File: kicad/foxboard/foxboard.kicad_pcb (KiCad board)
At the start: 2 copper layers, 40.2 x 15 mm, 184 parts, among them J2 USB_C_Receptacle_USB2.0, K1 KEYSW, K10 KEYSW, K11 KEYSW, K12 KEYSW, K13 KEYSW, K14 KEYSW, K15 KEYSW, K16 KEYSW, K17 KEYSW, K18 KEYSW, K19 KEYSW, K2 KEYSW, K20 KEYSW, K21 KEYSW, K22 KEYSW, K23 KEYSW, K24 KEYSW, K25 KEYSW, K26 KEYSW, K27 KEYSW, K28 KEYSW, K29 KEYSW, K3 KEYSW, K30 KEYSW, K31 KEYSW, K32 KEYSW, K33 KEYSW, K34 KEYSW, K35 KEYSW, K36 KEYSW, K38 KEYSW, K39 KEYSW, K4 KEYSW, K40 KEYSW, K41 KEYSW, K42 KEYSW, K43 KEYSW, K44 KEYSW, K45 KEYSW, K46 KEYSW, K47 KEYSW, K48 KEYSW, K49 KEYSW, K5 KEYSW, K50 KEYSW, K51 KEYSW, K52 KEYSW, K53 KEYSW, K54 KEYSW, K55 KEYSW, K56 KEYSW, K57 KEYSW, K58 KEYSW, K59 KEYSW, K6 KEYSW, K60 KEYSW, K61 KEYSW, K62 KEYSW, K63 KEYSW, K64 KEYSW, K65 KEYSW, K66 KEYSW, K67 KEYSW, K68 KEYSW, K69 KEYSW, K7 KEYSW, K70 KEYSW, K71 KEYSW, K72 KEYSW, K73 KEYSW, K74 KEYSW, K75 KEYSW, K76 KEYSW, K77 KEYSW, K78 KEYSW, K79 KEYSW, K8 KEYSW, K80 KEYSW, K81 KEYSW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

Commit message: add few cols & update eeschema
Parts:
- removed the D37 at (257.0, 297.2)
- added K37: KEYSW, PCM_marbastlib-mx:SW_MX_1u, F.Cu at (241.3, 307.3)
- added REF**: STAB_MX_2u, PCM_marbastlib-mx:STAB_MX_2u, F.Cu at (243.8, 266.7)
- added REF**: STAB_MX_2.25u, PCM_marbastlib-mx:STAB_MX_2.25u, F.Cu at (241.3, 304.8)
- added REF**: STAB_MX_2.25u, PCM_marbastlib-mx:STAB_MX_2.25u, F.Cu at (-2.54, 325.1)
- added REF**: STAB_MX_2.75u, PCM_marbastlib-mx:STAB_MX_2.75u, F.Cu at (236.2, 325.1)
- D37: moved to B.Cu
- K12, K23: footprint PCM_marbastlib-xp-plate-mx:Plate_MX_SPLIT-RSHIFT -> PCM_marbastlib-mx:SW_MX_1u
- K25: footprint PCM_marbastlib-mx:STAB_MX_2.25u -> PCM_marbastlib-mx:SW_MX_1u
- K69: footprint PCM_marbastlib-mx:STAB_MX_2.75u -> PCM_marbastlib-mx:SW_MX_1u
- moved D37 393.8 mm to (257.0, 299.7), turned to 180 degrees
- moved K12 2.54 mm to (-2.54, 325.1)
- moved K38 1.07 mm to (-10.2, 287.1)
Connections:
- K10 pad 1: Net-(K10-Pad1) -> Net-(U2-36_CS)
- K24 pad 1: Net-(K10-Pad1) -> Net-(U2-36_CS)
- K36 pad 1: Net-(K23-Pad1) -> Net-(U2-39_MISO1_OUT1A)
- K38 pad 1: Net-(K13-Pad1) -> Net-(K1-Pad1)
- K39 pad 1: Net-(K14-Pad1) -> Net-(K13-Pad1)
- K49 pad 1: Net-(K23-Pad1) -> Net-(U2-39_MISO1_OUT1A)
- K50 pad 1: Net-(K37-Pad1) -> Net-(U2-29_TX7)
- K51 pad 1: Net-(K51-Pad1) -> Net-(U2-38_CS1_IN1)
- K52 pad 1: Net-(K52-Pad1) -> Net-(U2-37_CS)
- K53 pad 1: Net-(K10-Pad1) -> Net-(U2-36_CS)
- K54 pad 1: Net-(K1-Pad1) -> Net-(U2-35_TX8)
- K55 pad 1: Net-(K13-Pad1) -> Net-(K1-Pad1)
- K56 pad 1: Net-(K14-Pad1) -> Net-(K13-Pad1)
- K66 pad 1: Net-(K23-Pad1) -> Net-(U2-39_MISO1_OUT1A)
- K67 pad 1: Net-(K37-Pad1) -> Net-(U2-29_TX7)
- K68 pad 1: Net-(K51-Pad1) -> Net-(U2-36_CS)
- K8 pad 1: Net-(K23-Pad1) -> Net-(U2-39_MISO1_OUT1A)
- K81 pad 1: unconnected-(K81-Pad1) -> Net-(U2-39_MISO1_OUT1A)
- K82 pad 1: unconnected-(K82-Pad1) -> Net-(U2-29_TX7)
- K83 pad 1: Net-(K51-Pad1) -> Net-(U2-38_CS1_IN1)
- K84 pad 1: Net-(K52-Pad1) -> Net-(U2-37_CS)
- K85 pad 1: Net-(K10-Pad1) -> Net-(U2-36_CS)
- K87 pad 1: Net-(K52-Pad1) -> Net-(U2-37_CS)
- K9 pad 1: Net-(K52-Pad1) -> Net-(U2-37_CS)
- U2 pad 21: unconnected-(U2-29_TX7-Pad21) -> Net-(U2-29_TX7)
- U2 pad 28: unconnected-(U2-36_CS-Pad28) -> Net-(U2-36_CS)
- U2 pad 29: unconnected-(U2-37_CS-Pad29) -> Net-(U2-37_CS)
- U2 pad 30: unconnected-(U2-38_CS1_IN1-Pad30) -> Net-(U2-38_CS1_IN1)
- U2 pad 31: unconnected-(U2-39_MISO1_OUT1A-Pad31) -> Net-(U2-39_MISO1_OUT1A)
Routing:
- net Net-(U2-39_MISO1_OUT1A): track 0.00 -> 304.2 mm
- net Net-(U2-29_TX7): track 0.00 -> 177.7 mm
- net Net-(U2-37_CS): track 0.00 -> 174.4 mm
- net Net-(U2-38_CS1_IN1): track 0.00 -> 156.2 mm
- net Net-(U2-36_CS): track 0.00 -> 153.0 mm
- net Net-(K13-Pad1): track 0.00 -> 131.7 mm
- net Net-(K14-Pad1): track 0.00 -> 127.9 mm
- net Net-(K1-Pad1): track 0.00 -> 114.4 mm
- net Net-(U2-35_TX8): track 28.7 -> 116.7 mm
- net Net-(K15-Pad1): track 0.00 -> 67.1 mm
- net Net-(D23-A): track 0.00 -> 22.8 mm
- net Net-(D38-K): track 368.0 -> 366.4 mm
- net Net-(D71-K): track 450.5 -> 451.4 mm
- net Net-(D25-K): track 311.4 -> 310.9 mm
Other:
- board outline removed

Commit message: add finish cols and usbc & update eeschema
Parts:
- removed C3, C4, C5, C6: 0.1u, Capacitor_SMD:C_0201_0603Metric_Pad0.64x0.40mm_HandSolder
- removed C7: 4.7u, Capacitor_SMD:C_0201_0603Metric_Pad0.64x0.40mm_HandSolder
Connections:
- K1 pad 1: Net-(K1-Pad1) -> Net-(U2-12_MISO_MQSL)
- K12 pad 1: Net-(K1-Pad1) -> Net-(U2-12_MISO_MQSL)
- K13 pad 1: Net-(K13-Pad1) -> Net-(U2-14_A0_TX3_SPDIF_OUT)
- K14 pad 1: Net-(K14-Pad1) -> Net-(U2-13_SCK_LED)
- K17 pad 1: Net-(K17-Pad1) -> Net-(U2-41_A17)
- K18 pad 1: Net-(K18-Pad1) -> Net-(U2-24_A10_TX6_SCL2)
- K19 pad 1: Net-(K19-Pad1) -> Net-(U2-40_A16)
- K2 pad 1: Net-(K13-Pad1) -> Net-(U2-14_A0_TX3_SPDIF_OUT)
- K20 pad 1: Net-(K20-Pad1) -> Net-(U2-39_MISO1_OUT1A)
- K21 pad 1: Net-(K21-Pad1) -> Net-(U2-26_A12_MOSI1)
- K22 pad 1: Net-(K22-Pad1) -> Net-(U2-27_A13_SCK1)
- K23 pad 1: Net-(U2-39_MISO1_OUT1A) -> Net-(U2-28_RX7)
- K25 pad 1: Net-(K1-Pad1) -> Net-(U2-12_MISO_MQSL)
- K26 pad 1: Net-(K13-Pad1) -> Net-(U2-14_A0_TX3_SPDIF_OUT)
- K27 pad 1: Net-(K14-Pad1) -> Net-(U2-13_SCK_LED)
- K3 pad 1: Net-(K14-Pad1) -> Net-(U2-13_SCK_LED)
- K30 pad 1: Net-(K17-Pad1) -> Net-(U2-41_A17)
- K31 pad 1: Net-(K18-Pad1) -> Net-(U2-24_A10_TX6_SCL2)
- K32 pad 1: Net-(K19-Pad1) -> Net-(U2-40_A16)
- K33 pad 1: Net-(K20-Pad1) -> Net-(U2-39_MISO1_OUT1A)
- K34 pad 1: Net-(K21-Pad1) -> Net-(U2-26_A12_MOSI1)
- K35 pad 1: Net-(K22-Pad1) -> Net-(U2-27_A13_SCK1)
- K36 pad 1: Net-(U2-39_MISO1_OUT1A) -> Net-(U2-28_RX7)
- K38 pad 1: Net-(K1-Pad1) -> Net-(U2-12_MISO_MQSL)
- K39 pad 1: Net-(K13-Pad1) -> Net-(U2-14_A0_TX3_SPDIF_OUT)
- K4 pad 1: Net-(K17-Pad1) -> Net-(U2-41_A17)
- K40 pad 1: Net-(K14-Pad1) -> Net-(U2-13_SCK_LED)
- K43 pad 1: Net-(K17-Pad1) -> Net-(U2-41_A17)
- K44 pad 1: Net-(K18-Pad1) -> Net-(U2-24_A10_TX6_SCL2)
- K45 pad 1: Net-(K19-Pad1) -> Net-(U2-40_A16)
- K46 pad 1: Net-(K20-Pad1) -> Net-(U2-39_MISO1_OUT1A)
- K47 pad 1: Net-(K21-Pad1) -> Net-(U2-26_A12_MOSI1)
- K48 pad 1: Net-(K22-Pad1) -> Net-(U2-27_A13_SCK1)
- K49 pad 1: Net-(U2-39_MISO1_OUT1A) -> Net-(U2-28_RX7)
- K5 pad 1: Net-(K20-Pad1) -> Net-(U2-39_MISO1_OUT1A)
- K55 pad 1: Net-(K1-Pad1) -> Net-(U2-12_MISO_MQSL)
- K56 pad 1: Net-(K13-Pad1) -> Net-(U2-14_A0_TX3_SPDIF_OUT)
- K57 pad 1: Net-(K14-Pad1) -> Net-(U2-13_SCK_LED)
- K6 pad 1: Net-(K21-Pad1) -> Net-(U2-26_A12_MOSI1)
- K60 pad 1: Net-(K17-Pad1) -> Net-(U2-41_A17)
- K61 pad 1: Net-(K18-Pad1) -> Net-(U2-24_A10_TX6_SCL2)
- K62 pad 1: Net-(K19-Pad1) -> Net-(U2-40_A16)
- K63 pad 1: Net-(K20-Pad1) -> Net-(U2-39_MISO1_OUT1A)
- K64 pad 1: Net-(K21-Pad1) -> Net-(U2-26_A12_MOSI1)
- K65 pad 1: Net-(K22-Pad1) -> Net-(U2-27_A13_SCK1)
- K66 pad 1: Net-(U2-39_MISO1_OUT1A) -> Net-(U2-28_RX7)
- K7 pad 1: Net-(K22-Pad1) -> Net-(U2-27_A13_SCK1)
- K71 pad 1: Net-(K1-Pad1) -> Net-(U2-12_MISO_MQSL)
- K72 pad 1: Net-(K13-Pad1) -> Net-(U2-14_A0_TX3_SPDIF_OUT)
- K73 pad 1: Net-(K14-Pad1) -> Net-(U2-13_SCK_LED)
- K75 pad 1: Net-(K17-Pad1) -> Net-(U2-41_A17)
- K76 pad 1: Net-(K18-Pad1) -> Net-(U2-24_A10_TX6_SCL2)
- K77 pad 1: Net-(K19-Pad1) -> Net-(U2-40_A16)
- K78 pad 1: Net-(K20-Pad1) -> Net-(U2-39_MISO1_OUT1A)
- K79 pad 1: Net-(K21-Pad1) -> Net-(U2-26_A12_MOSI1)
- K8 pad 1: Net-(U2-39_MISO1_OUT1A) -> Net-(U2-28_RX7)
- K80 pad 1: Net-(K22-Pad1) -> Net-(U2-27_A13_SCK1)
- K81 pad 1: Net-(U2-39_MISO1_OUT1A) -> Net-(U2-28_RX7)
- U2 pad 14: unconnected-(U2-12_MISO_MQSL-Pad14) -> Net-(U2-12_MISO_MQSL)
- U2 pad 15: unconnected-(U2-3V3-Pad15) -> Net-(K15-Pad1)
- U2 pad 16: unconnected-(U2-24_A10_TX6_SCL2-Pad16) -> Net-(U2-24_A10_TX6_SCL2)
- U2 pad 18: unconnected-(U2-26_A12_MOSI1-Pad18) -> Net-(U2-26_A12_MOSI1)
- U2 pad 19: unconnected-(U2-27_A13_SCK1-Pad19) -> Net-(U2-27_A13_SCK1)
- U2 pad 20: unconnected-(U2-28_RX7-Pad20) -> Net-(U2-28_RX7)
- U2 pad 32: unconnected-(U2-40_A16-Pad32) -> Net-(U2-40_A16)
- U2 pad 33: unconnected-(U2-41_A17-Pad33) -> Net-(U2-41_A17)
- U2 pad 34: unconnected-(U2-GND-Pad34) -> Net-(K16-Pad1)
- U2 pad 35: unconnected-(U2-13_SCK_LED-Pad35) -> Net-(U2-13_SCK_LED)
- U2 pad 36: unconnected-(U2-14_A0_TX3_SPDIF_OUT-Pad36) -> Net-(U2-14_A0_TX3_SPDIF_OUT)
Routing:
- net Net-(J2-D+-PadA6): track 0.00 -> 914.7 mm, vias 0 -> 5
- net Net-(J2-D--PadA7): track 0.00 -> 485.6 mm, vias 0 -> 3
- net Net-(U2-14_A0_TX3_SPDIF_OUT): track 0.00 -> 478.1 mm, vias 0 -> 2
- net Net-(U2-13_SCK_LED): track 0.00 -> 467.3 mm, vias 0 -> 1
- net Net-(U2-12_MISO_MQSL): track 0.00 -> 452.4 mm, vias 0 -> 4
- net Net-(U2-41_A17): track 0.00 -> 429.7 mm, vias 0 -> 3
- net Net-(U2-40_A16): track 0.00 -> 401.7 mm, vias 0 -> 1
- net Net-(J2-SHIELD): track 0.00 -> 367.8 mm, vias 0 -> 4
- net Net-(U2-VIN): track 0.00 -> 361.1 mm, vias 0 -> 7
- net Net-(U2-24_A10_TX6_SCL2): track 0.00 -> 294.8 mm, vias 0 -> 1
- net Net-(U2-26_A12_MOSI1): track 0.00 -> 254.0 mm, vias 0 -> 2
- net Net-(K16-Pad1): track 95.7 -> 342.0 mm, vias 0 -> 2
- net Net-(K15-Pad1): track 67.1 -> 313.0 mm, vias 0 -> 2
- net Net-(U2-27_A13_SCK1): track 0.00 -> 238.6 mm, vias 0 -> 2
- net Net-(U2-28_RX7): track 0.00 -> 228.8 mm, vias 0 -> 2
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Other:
- board outline added: 365.8 x 142.2 mm
- board text removed: "FoxBoard by Lunarequest"

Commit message: move teensy a little back
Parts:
- moved U2 2.86 mm to (295.6, 306.1)
- moved REF** 0.63 mm to (236.2, 324.5)
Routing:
- net Net-(U2-37_CS): track 174.4 -> 483.7 mm
- net Net-(D37-A): track 0.00 -> 13.8 mm
- net Net-(D25-K): track 310.9 -> 320.9 mm
- net Net-(U2-35_TX8): track 116.7 -> 123.5 mm
- net Net-(D36-A): track 0.00 -> 6.77 mm
- net Net-(D1-K): track 356.0 -> 362.6 mm
- net Net-(D66-A): track 0.00 -> 5.72 mm
- net Net-(U2-28_RX7): track 228.8 -> 223.8 mm
- net Net-(J2-D--PadA7): track 485.6 -> 481.1 mm
- net Net-(D38-K): track 367.8 -> 372.3 mm, vias 0 -> 2
- net Net-(U2-29_TX7): track 177.7 -> 181.8 mm
- net Net-(D12-K): track 314.5 -> 318.5 mm
- net Net-(D69-A): track 0.00 -> 3.60 mm
- net Net-(D55-K): track 383.4 -> 386.9 mm
- net Net-(U2-12_MISO_MQSL): track 452.4 -> 455.4 mm
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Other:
- outline, holes or cut-outs redrawn

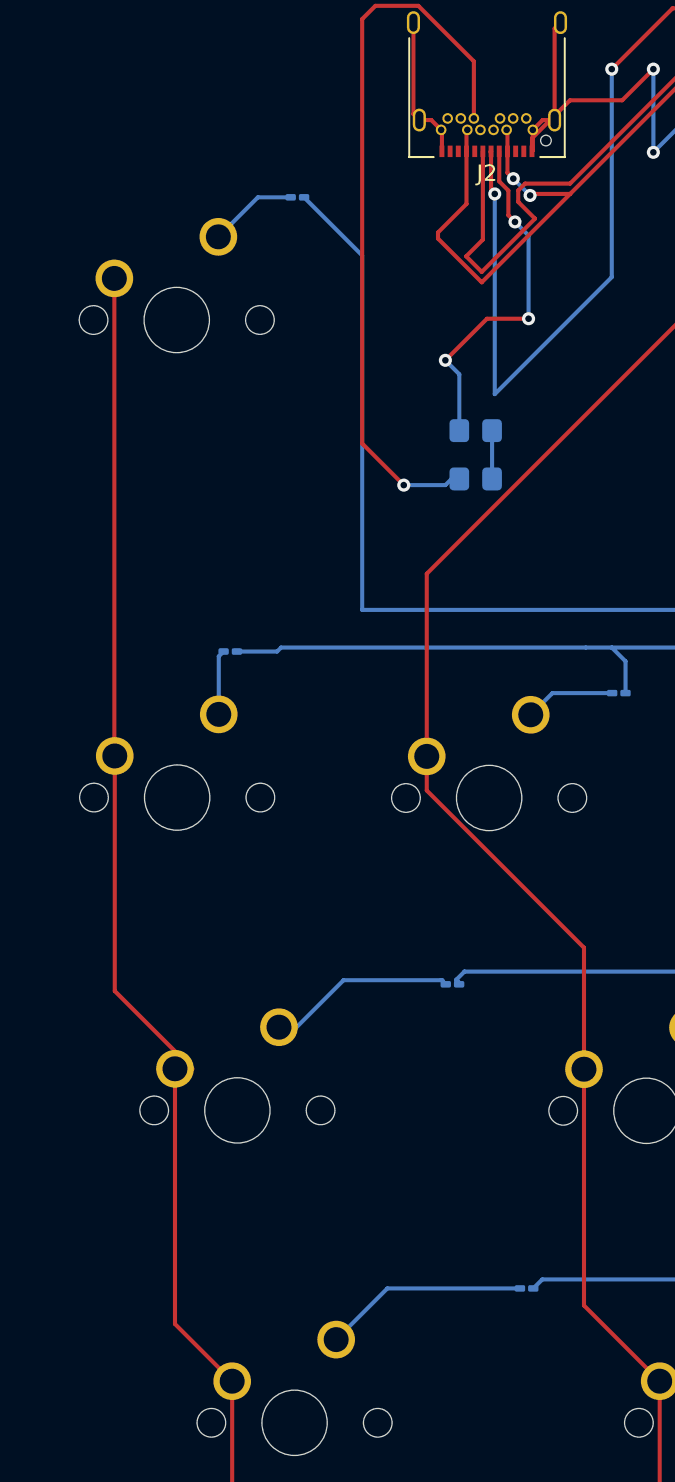
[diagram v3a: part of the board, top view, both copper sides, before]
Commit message: hook up resistor to ground
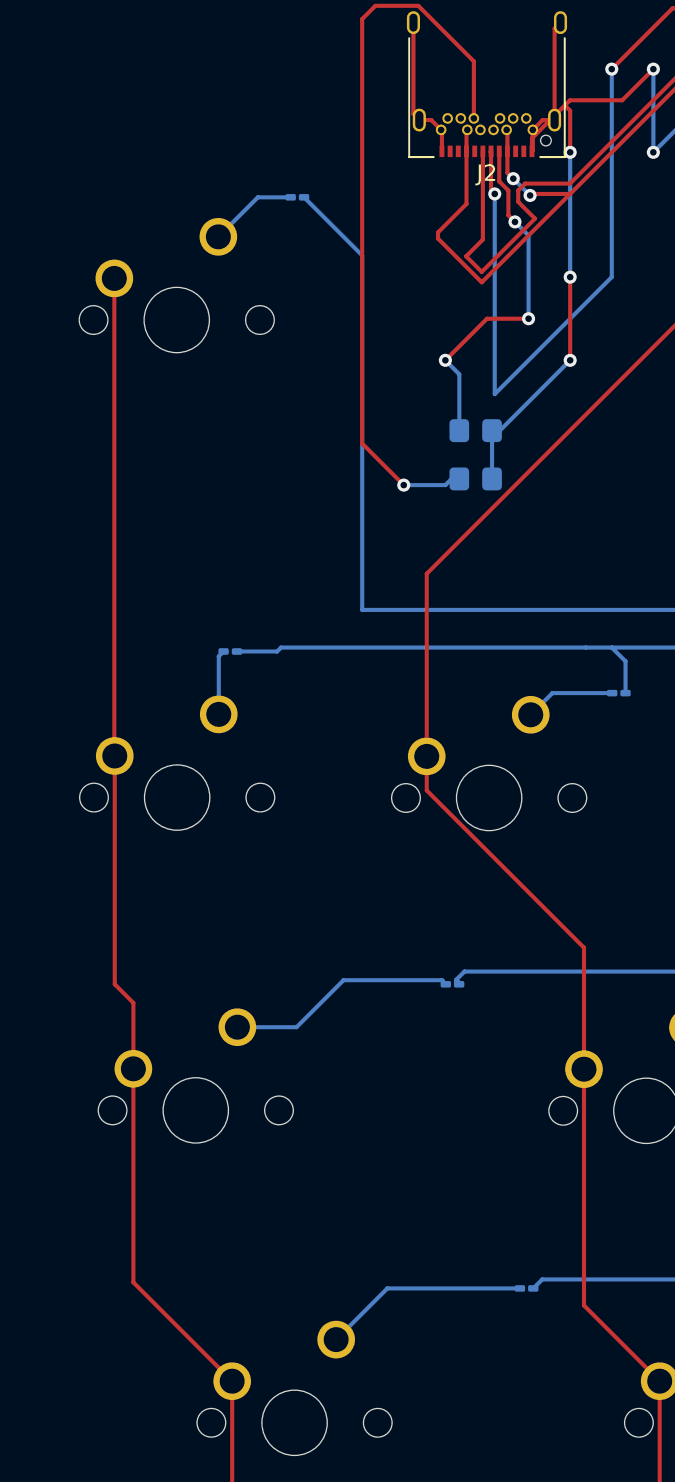
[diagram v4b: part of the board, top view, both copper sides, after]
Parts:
- moved K38 2.54 mm to (-12.7, 287.1)
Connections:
- net Net-(U2-VIN) renamed VBUS
- J2 pad A1: Net-(J2-SHIELD) -> GND
- J2 pad A12: Net-(J2-SHIELD) -> GND
- J2 pad B1: Net-(J2-SHIELD) -> GND
- J2 pad B12: Net-(J2-SHIELD) -> GND
- J2 pad S1: Net-(J2-SHIELD) -> GND
- K52 pad 1: Net-(U2-37_CS) -> Net-(D9-A)
- K84 pad 1: Net-(U2-37_CS) -> Net-(D9-A)
- K87 pad 1: Net-(U2-37_CS) -> Net-(D9-A)
- K9 pad 1: Net-(U2-37_CS) -> Net-(D9-A)
- R5 pad 1: +5V -> GND
- R5 pad 2: Net-(J2-CC1) -> Net-(J2-CC2)
- R6 pad 1: +5V -> GND
- R6 pad 2: Net-(J2-CC2) -> Net-(J2-CC1)
- U2 pad 29: Net-(U2-37_CS) -> Net-(D9-A)
- U2 pad 47: Net-(J2-SHIELD) -> GND
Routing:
- net Net-(U2-37_CS): track 483.7 -> 0.00 mm
- net Net-(D9-A): track 5.52 -> 489.2 mm
- net GND: track 0.00 -> 394.0 mm, vias 0 -> 7
- net Net-(J2-SHIELD): track 368.6 -> 0.00 mm, vias 4 -> 0
- net Net-(D38-A): track 10.5 -> 14.1 mm
- net +5V: track 3.14 -> 0.00 mm

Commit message: switch to better layout
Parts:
- removed REF**: STAB_MX_6.25u, PCM_marbastlib-mx:STAB_MX_6.25u
- removed REF**: STAB_MX_2u, PCM_marbastlib-mx:STAB_MX_2u
- removed REF** (x2): STAB_MX_2.25u, PCM_marbastlib-mx:STAB_MX_2.25u
- removed REF**: STAB_MX_2.75u, PCM_marbastlib-mx:STAB_MX_2.75u
- added S30: BACKSPACE, PCM_marbastlib-mx:STAB_MX_2u, F.Cu at (283.8, 275.0)
- added S63: ANSI_ENTER, PCM_marbastlib-mx:STAB_MX_2.25u, F.Cu at (281.5, 313.1)
- added S64: LShift, PCM_marbastlib-mx:STAB_MX_2.25u, F.Cu at (38.6, 332.1)
- added S75: RSHIFT, PCM_marbastlib-mx:STAB_MX_P_2.75u, F.Cu at (276.7, 332.1)
- added S80: 7u_SPACE, PCM_marbastlib-mx:STAB_MX_P_6.25u, F.Cu at (148.1, 351.2)
- K1, K2, K3, K5, K6, K7, K8: footprint PCM_marbastlib-mx:SW_MX_1.25u -> PCM_marbastlib-mx:SW_MX_1u
- K15, K77, K78, K79, K81, K82, K83, K9: footprint PCM_marbastlib-mx:SW_MX_1u -> PCM_marbastlib-mx:SW_MX_1.25u
- K34, K47: footprint PCM_marbastlib-mx:SW_MX_1u -> PCM_marbastlib-mx:SW_MX_1.5u
- K38: footprint PCM_marbastlib-mx:SW_MX_1.75u -> PCM_marbastlib-mx:SW_MX_1u
- K4: footprint rhais_cherry:MX_KEY_4.45 -> PCM_marbastlib-mx:SW_MX_1u
- U2: moved to B.Cu
- moved K12 287.8 mm to (274.3, 246.4)
- moved K16 280.4 mm to (355.3, 246.4)
- moved K15 280.3 mm to (336.2, 246.4)
- moved K14 280.2 mm to (317.2, 246.4)
- moved D16 279.5 mm to (361.9, 238.7)
- moved D14 279.4 mm to (323.8, 238.7)
- moved D15 279.3 mm to (342.9, 238.7)
- moved D12 276.7 mm to (281.0, 238.7)
- moved K13 275.7 mm to (293.4, 246.4)
- moved D13 275.5 mm to (300.0, 238.7)
- moved K76 244.5 mm to (336.2, 332.1)
- moved D76 243.4 mm to (342.9, 324.4)
- moved D51 219.8 mm to (40.5, 305.4)
- moved K71 218.6 mm to (183.8, 332.1)
- moved K53 218.2 mm to (79.1, 313.1)
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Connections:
- D1 pad 1: Net-(D1-K) -> row 1
- D10 pad 1: Net-(D1-K) -> row 1
- D11 pad 1: Net-(D1-K) -> row 1
- D12 pad 1: Net-(D12-K) -> row 1
- D13 pad 1: Net-(D12-K) -> row 1
- D14 pad 1: Net-(D12-K) -> row 1
- D15 pad 1: Net-(D12-K) -> row 1
- D16 pad 1: Net-(D12-K) -> row 1
- D17 pad 1: Net-(D12-K) -> row 2
- D18 pad 1: Net-(D12-K) -> row 2
- D19 pad 1: Net-(D12-K) -> row 2
- D2 pad 1: Net-(D1-K) -> row 1
- D20 pad 1: Net-(D12-K) -> row 2
- D21 pad 1: Net-(D12-K) -> row 2
- D22 pad 1: Net-(D12-K) -> row 2
- D23 pad 1: Net-(D12-K) -> row 2
- D24 pad 1: Net-(D12-K) -> row 2
- D25 pad 1: Net-(D25-K) -> row 2
- D26 pad 1: Net-(D25-K) -> row 2
- D27 pad 1: Net-(D25-K) -> row 2
- D28 pad 1: Net-(D25-K) -> row 2
- D29 pad 1: Net-(D25-K) -> row 2
- D3 pad 1: Net-(D1-K) -> row 1
- D30 pad 1: Net-(D25-K) -> row 2
- D31 pad 1: Net-(D25-K) -> row 2
- D32 pad 1: Net-(D25-K) -> row 2
- D33 pad 1: Net-(D25-K) -> row 2
- D34 pad 1: Net-(D25-K) -> row 3
- D35 pad 1: Net-(D25-K) -> row 3
- D36 pad 1: Net-(D25-K) -> row 3
- D37 pad 1: Net-(D25-K) -> row 3
- D38 pad 1: Net-(D38-K) -> row 3
- D39 pad 1: Net-(D38-K) -> row 3
- D4 pad 1: Net-(D1-K) -> row 1
- D40 pad 1: Net-(D38-K) -> row 3
- D41 pad 1: Net-(D38-K) -> row 3
- D42 pad 1: Net-(D38-K) -> row 3
- D43 pad 1: Net-(D38-K) -> row 3
- D44 pad 1: Net-(D38-K) -> row 3
- D45 pad 1: Net-(D38-K) -> row 3
- D46 pad 1: Net-(D38-K) -> row 3
- D47 pad 1: Net-(D38-K) -> row 3
- D48 pad 1: Net-(D38-K) -> row 3
- D49 pad 1: Net-(D38-K) -> row 3
- D5 pad 1: Net-(D1-K) -> row 1
- D50 pad 1: Net-(D38-K) -> row 3
- D51 pad 1: Net-(D38-K) -> row 4
- D52 pad 1: Net-(D38-K) -> row 4
- D53 pad 1: Net-(D38-K) -> row 4
- D54 pad 1: Net-(D38-K) -> row 4
- D55 pad 1: Net-(D55-K) -> row 4
- D56 pad 1: Net-(D55-K) -> row 4
- D57 pad 1: Net-(D55-K) -> row 4
- D58 pad 1: Net-(D55-K) -> row 4
- D59 pad 1: Net-(D55-K) -> row 4
- D6 pad 1: Net-(D1-K) -> row 1
- D60 pad 1: Net-(D55-K) -> row 4
- D61 pad 1: Net-(D55-K) -> row 4
- D62 pad 1: Net-(D55-K) -> row 4
- D63 pad 1: Net-(D55-K) -> row 4
- D64 pad 1: Net-(D55-K) -> row 5
- D65 pad 1: Net-(D55-K) -> row 5
- D66 pad 1: Net-(D55-K) -> row 5
- D67 pad 1: Net-(D55-K) -> row 5
- D68 pad 1: Net-(D55-K) -> row 5
- D69 pad 1: Net-(D55-K) -> row 5
- D7 pad 1: Net-(D1-K) -> row 1
- D70 pad 1: Net-(D55-K) -> row 5
- D71 pad 1: Net-(D71-K) -> row 5
- D72 pad 1: Net-(D71-K) -> row 5
- D73 pad 1: Net-(D71-K) -> row 5
- D74 pad 1: Net-(D71-K) -> row 5
- D75 pad 1: Net-(D71-K) -> row 5
- D76 pad 1: Net-(D71-K) -> row 5
- D77 pad 1: Net-(D71-K) -> row 6
- D78 pad 1: Net-(D71-K) -> row 6
- D79 pad 1: Net-(D71-K) -> row 6
- D8 pad 1: Net-(D1-K) -> row 1
- D80 pad 1: Net-(D71-K) -> row 6
- D81 pad 1: Net-(D71-K) -> row 6
- D82 pad 1: Net-(D71-K) -> row 6
- D83 pad 1: Net-(D71-K) -> row 6
- D84 pad 1: Net-(D71-K) -> row 6
- D85 pad 1: Net-(D71-K) -> row 6
- D86 pad 1: Net-(D71-K) -> row 6
- D87 pad 1: Net-(D55-K) -> row 6
- D9 pad 1: Net-(D1-K) -> row 1
- K1 pad 1: Net-(U2-12_MISO_MQSL) -> col 1
- K10 pad 1: Net-(U2-36_CS) -> col 11
- K11 pad 1: Net-(U2-35_TX8) -> col 12
- K12 pad 1: Net-(U2-12_MISO_MQSL) -> col 13
- K13 pad 1: Net-(U2-14_A0_TX3_SPDIF_OUT) -> col 14
- K14 pad 1: Net-(U2-13_SCK_LED) -> col 15
- K15 pad 1: Net-(K15-Pad1) -> col 16
- K16 pad 1: Net-(K16-Pad1) -> col 17
- K17 pad 1: Net-(U2-41_A17) -> col 1
- K18 pad 1: Net-(U2-24_A10_TX6_SCL2) -> col 2
- K19 pad 1: Net-(U2-40_A16) -> col 3
- K2 pad 1: Net-(U2-14_A0_TX3_SPDIF_OUT) -> col 3
- K20 pad 1: Net-(U2-39_MISO1_OUT1A) -> col 4
- K21 pad 1: Net-(U2-26_A12_MOSI1) -> col 5
- K22 pad 1: Net-(U2-27_A13_SCK1) -> col 6
- K23 pad 1: Net-(U2-28_RX7) -> col 7
- K24 pad 1: Net-(U2-36_CS) -> col 8
- K25 pad 1: Net-(U2-12_MISO_MQSL) -> col 9
- K26 pad 1: Net-(U2-14_A0_TX3_SPDIF_OUT) -> col 10
- K27 pad 1: Net-(U2-13_SCK_LED) -> col 11
- K28 pad 1: Net-(K15-Pad1) -> col 12
- K29 pad 1: Net-(K16-Pad1) -> col 13
- K3 pad 1: Net-(U2-13_SCK_LED) -> col 4
- K30 pad 1: Net-(U2-41_A17) -> col 14
- K31 pad 1: Net-(U2-24_A10_TX6_SCL2) -> col 15
- K32 pad 1: Net-(U2-40_A16) -> col 16
- K33 pad 1: Net-(U2-39_MISO1_OUT1A) -> col 17
- K34 pad 1: Net-(U2-26_A12_MOSI1) -> col 1
- K35 pad 1: Net-(U2-27_A13_SCK1) -> col 2
- K36 pad 1: Net-(U2-28_RX7) -> col 3
- K37 pad 1: Net-(U2-38_CS1_IN1) -> col 4
- K38 pad 1: Net-(U2-12_MISO_MQSL) -> col 5
- K39 pad 1: Net-(U2-14_A0_TX3_SPDIF_OUT) -> col 6
- K4 pad 1: Net-(U2-41_A17) -> col 5
- K40 pad 1: Net-(U2-13_SCK_LED) -> col 7
- K41 pad 1: Net-(K15-Pad1) -> col 8
- K42 pad 1: Net-(K16-Pad1) -> col 9
- K43 pad 1: Net-(U2-41_A17) -> col 10
- K44 pad 1: Net-(U2-24_A10_TX6_SCL2) -> col 11
- K45 pad 1: Net-(U2-40_A16) -> col 12
- K46 pad 1: Net-(U2-39_MISO1_OUT1A) -> col 13
- K47 pad 1: Net-(U2-26_A12_MOSI1) -> col 14
- K48 pad 1: Net-(U2-27_A13_SCK1) -> col 15
- K49 pad 1: Net-(U2-28_RX7) -> col 16
- K5 pad 1: Net-(U2-39_MISO1_OUT1A) -> col 6
- K50 pad 1: Net-(U2-29_TX7) -> col 17
- K51 pad 1: Net-(U2-38_CS1_IN1) -> col 1
- K52 pad 1: Net-(D9-A) -> col 2
- K53 pad 1: Net-(U2-36_CS) -> col 3
- K54 pad 1: Net-(U2-35_TX8) -> col 4
- K55 pad 1: Net-(U2-12_MISO_MQSL) -> col 5
- K56 pad 1: Net-(U2-14_A0_TX3_SPDIF_OUT) -> col 6
- K57 pad 1: Net-(U2-13_SCK_LED) -> col 7
- K58 pad 1: Net-(K15-Pad1) -> col 8
- K59 pad 1: Net-(K16-Pad1) -> col 9
- K6 pad 1: Net-(U2-26_A12_MOSI1) -> col 7
- K60 pad 1: Net-(U2-41_A17) -> col 10
- K61 pad 1: Net-(U2-24_A10_TX6_SCL2) -> col 11
- K62 pad 1: Net-(U2-40_A16) -> col 12
- K63 pad 1: Net-(U2-39_MISO1_OUT1A) -> col 13
- K64 pad 1: Net-(U2-26_A12_MOSI1) -> col 1
- K65 pad 1: Net-(U2-27_A13_SCK1) -> col 2
- K66 pad 1: Net-(U2-28_RX7) -> col 3
- K67 pad 1: Net-(U2-29_TX7) -> col 4
- K68 pad 1: Net-(U2-36_CS) -> col 5
- K69 pad 1: Net-(U2-38_CS1_IN1) -> col 6
- K7 pad 1: Net-(U2-27_A13_SCK1) -> col 8
- K70 pad 1: Net-(U2-35_TX8) -> col 7
- K71 pad 1: Net-(U2-12_MISO_MQSL) -> col 8
- K72 pad 1: Net-(U2-14_A0_TX3_SPDIF_OUT) -> col 9
- K73 pad 1: Net-(U2-13_SCK_LED) -> col 10
- K74 pad 1: Net-(K16-Pad1) -> col 11
- K75 pad 1: Net-(U2-41_A17) -> col 13
- K76 pad 1: Net-(U2-24_A10_TX6_SCL2) -> col 16
- K77 pad 1: Net-(U2-40_A16) -> col 1
- K78 pad 1: Net-(U2-39_MISO1_OUT1A) -> col 2
- K79 pad 1: Net-(U2-26_A12_MOSI1) -> col 3
- K8 pad 1: Net-(U2-28_RX7) -> col 9
- K80 pad 1: Net-(U2-27_A13_SCK1) -> col 6
- K81 pad 1: Net-(U2-28_RX7) -> col 10
- K82 pad 1: Net-(U2-29_TX7) -> col 11
- K83 pad 1: Net-(U2-38_CS1_IN1) -> col 13
- K84 pad 1: Net-(D9-A) -> col 14
- K85 pad 1: Net-(U2-36_CS) -> col 15
- K86 pad 1: Net-(U2-35_TX8) -> col 16
- K87 pad 1: Net-(D9-A) -> col 17
- K9 pad 1: Net-(D9-A) -> col 10
- U2 pad 1: unconnected-(U2-GND-Pad1) -> row 6
- U2 pad 14: Net-(U2-12_MISO_MQSL) -> col 17
- U2 pad 15: Net-(K15-Pad1) -> unconnected-(U2-3V3-Pad15)
- U2 pad 16: Net-(U2-24_A10_TX6_SCL2) -> unconnected-(U2-24_A10_TX6_SCL2-Pad16)
- U2 pad 17: Net-(D25-K) -> unconnected-(U2-25_A11_RX6_SDA2-Pad17)
- U2 pad 18: Net-(U2-26_A12_MOSI1) -> col 14
- U2 pad 19: Net-(U2-27_A13_SCK1) -> col 10
- U2 pad 2: unconnected-(U2-0_RX1_CRX2_CS1-Pad2) -> row 5
- U2 pad 20: Net-(U2-28_RX7) -> col 8
- U2 pad 21: Net-(U2-29_TX7) -> col 7
- U2 pad 22: Net-(D38-K) -> col 6
- U2 pad 23: Net-(D12-K) -> col 5
- U2 pad 24: Net-(D1-K) -> col 4
- U2 pad 25: Net-(D71-K) -> row 4
- U2 pad 26: Net-(D55-K) -> col 2
- U2 pad 27: Net-(U2-35_TX8) -> col 11
- U2 pad 28: Net-(U2-36_CS) -> col 12
- U2 pad 29: Net-(D9-A) -> col 13
- U2 pad 3: unconnected-(U2-1_TX1_CTX2_MISO1-Pad3) -> col 1
- U2 pad 30: Net-(U2-38_CS1_IN1) -> col 9
- U2 pad 31: Net-(U2-39_MISO1_OUT1A) -> col 15
- U2 pad 32: Net-(U2-40_A16) -> unconnected-(U2-40_A16-Pad32)
- U2 pad 33: Net-(U2-41_A17) -> unconnected-(U2-41_A17-Pad33)
- U2 pad 34: Net-(K16-Pad1) -> unconnected-(U2-GND-Pad34)
- U2 pad 35: Net-(U2-13_SCK_LED) -> unconnected-(U2-13_SCK_LED-Pad35)
- U2 pad 36: Net-(U2-14_A0_TX3_SPDIF_OUT) -> col 16
- U2 pad 4: unconnected-(U2-2_OUT2-Pad4) -> col 3
- U2 pad 44: unconnected-(U2-22_A8_CTX1-Pad44) -> row 3
- U2 pad 45: unconnected-(U2-23_A9_CRX1_MCLK1-Pad45) -> row 2
- U2 pad 46: unconnected-(U2-3V3-Pad46) -> row 1
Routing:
- net col 1: track 0.00 -> 521.8 mm, vias 0 -> 2
- net Net-(J2-D+-PadA6): track 911.8 -> 400.7 mm, vias 5 -> 3
- net col 3: track 0.00 -> 497.5 mm, vias 0 -> 3
- net Net-(D9-A): track 489.2 -> 4.78 mm
- net Net-(U2-14_A0_TX3_SPDIF_OUT): track 480.9 -> 0.00 mm, vias 2 -> 0
- net Net-(U2-13_SCK_LED): track 468.5 -> 0.00 mm, vias 1 -> 0
- net Net-(U2-12_MISO_MQSL): track 454.9 -> 0.00 mm, vias 4 -> 0
- net Net-(D71-K): track 452.8 -> 0.00 mm, vias 2 -> 0
- net Net-(U2-41_A17): track 430.6 -> 0.00 mm, vias 3 -> 0
- net row 1: track 0.00 -> 420.0 mm
- net col 2: track 0.00 -> 409.0 mm
- net Net-(U2-40_A16): track 402.4 -> 0.00 mm, vias 1 -> 0
- net row 2: track 0.00 -> 401.6 mm
- net row 3: track 0.00 -> 392.6 mm
- net Net-(D55-K): track 386.9 -> 0.00 mm
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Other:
- board size 365.8 x 142.2 mm -> 360.7 x 139.7 mm
